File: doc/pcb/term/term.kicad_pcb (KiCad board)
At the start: 2 copper layers, 18 parts, among them U1 LM35-LP, U2 LM1117-3.3, U3 STM32F030F4Px, U4 CA56-12CGKWA

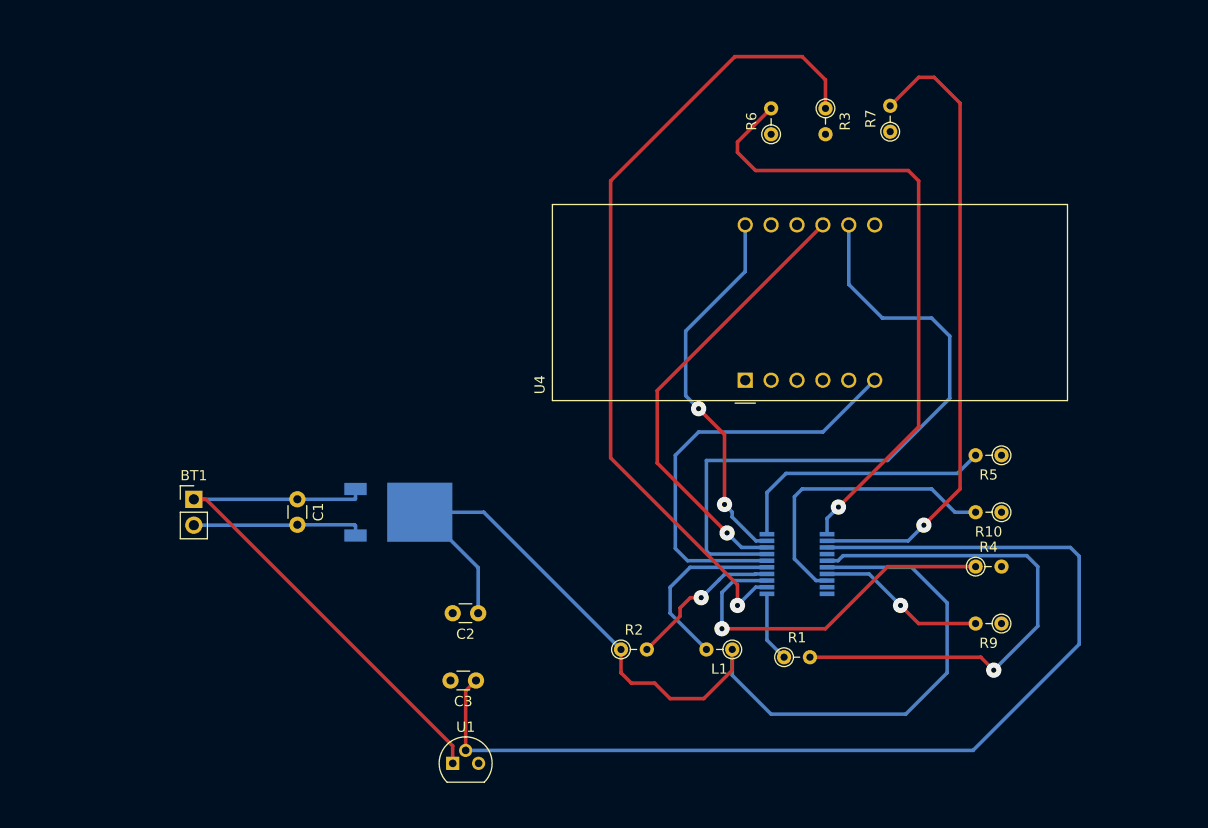
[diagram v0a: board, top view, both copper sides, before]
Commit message: pcb with logo
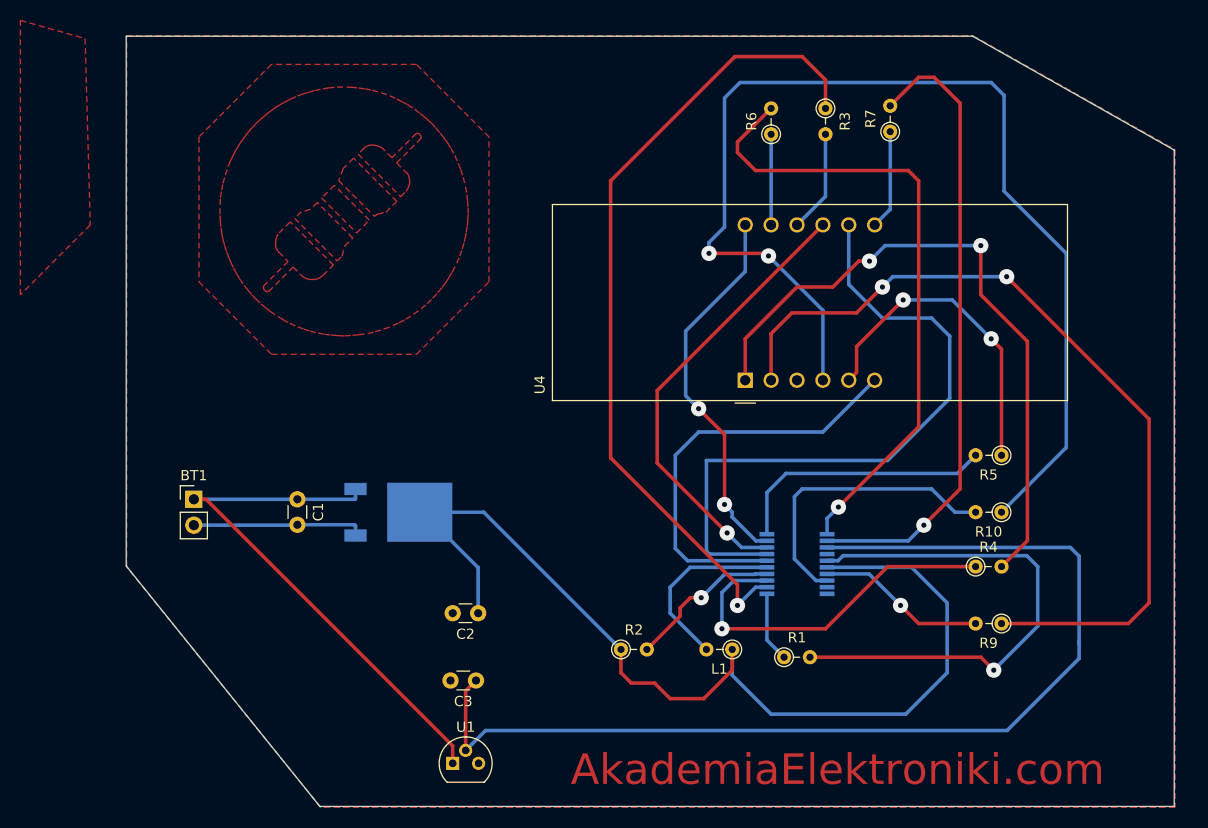
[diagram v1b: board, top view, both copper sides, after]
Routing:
- net SC: track 0.00 -> 110.9 mm, vias 0 -> 2
- net SD: track 0.00 -> 83.1 mm, vias 0 -> 2
- net SE: track 0.00 -> 65.4 mm, vias 0 -> 2
- net SG: track 0.00 -> 32.1 mm, vias 0 -> 2
- net SF: track 0.00 -> 10.0 mm
- net SB: track 0.00 -> 9.78 mm
- net SA: track 0.00 -> 8.89 mm
- net Net-(C3-Pad1): track 105.5 -> 106.6 mm
- added copper zone on F.Cu, net (none)
- added copper zone on B.Cu, net GND
- added copper zone on F.Cu, net GND
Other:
- board outline added: 102.8 x 75.6 mm
- board text added: "AkademiaElektroniki.com"
